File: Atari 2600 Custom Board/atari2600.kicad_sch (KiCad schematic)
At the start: 8 parts, among them SW1 B3F-4050

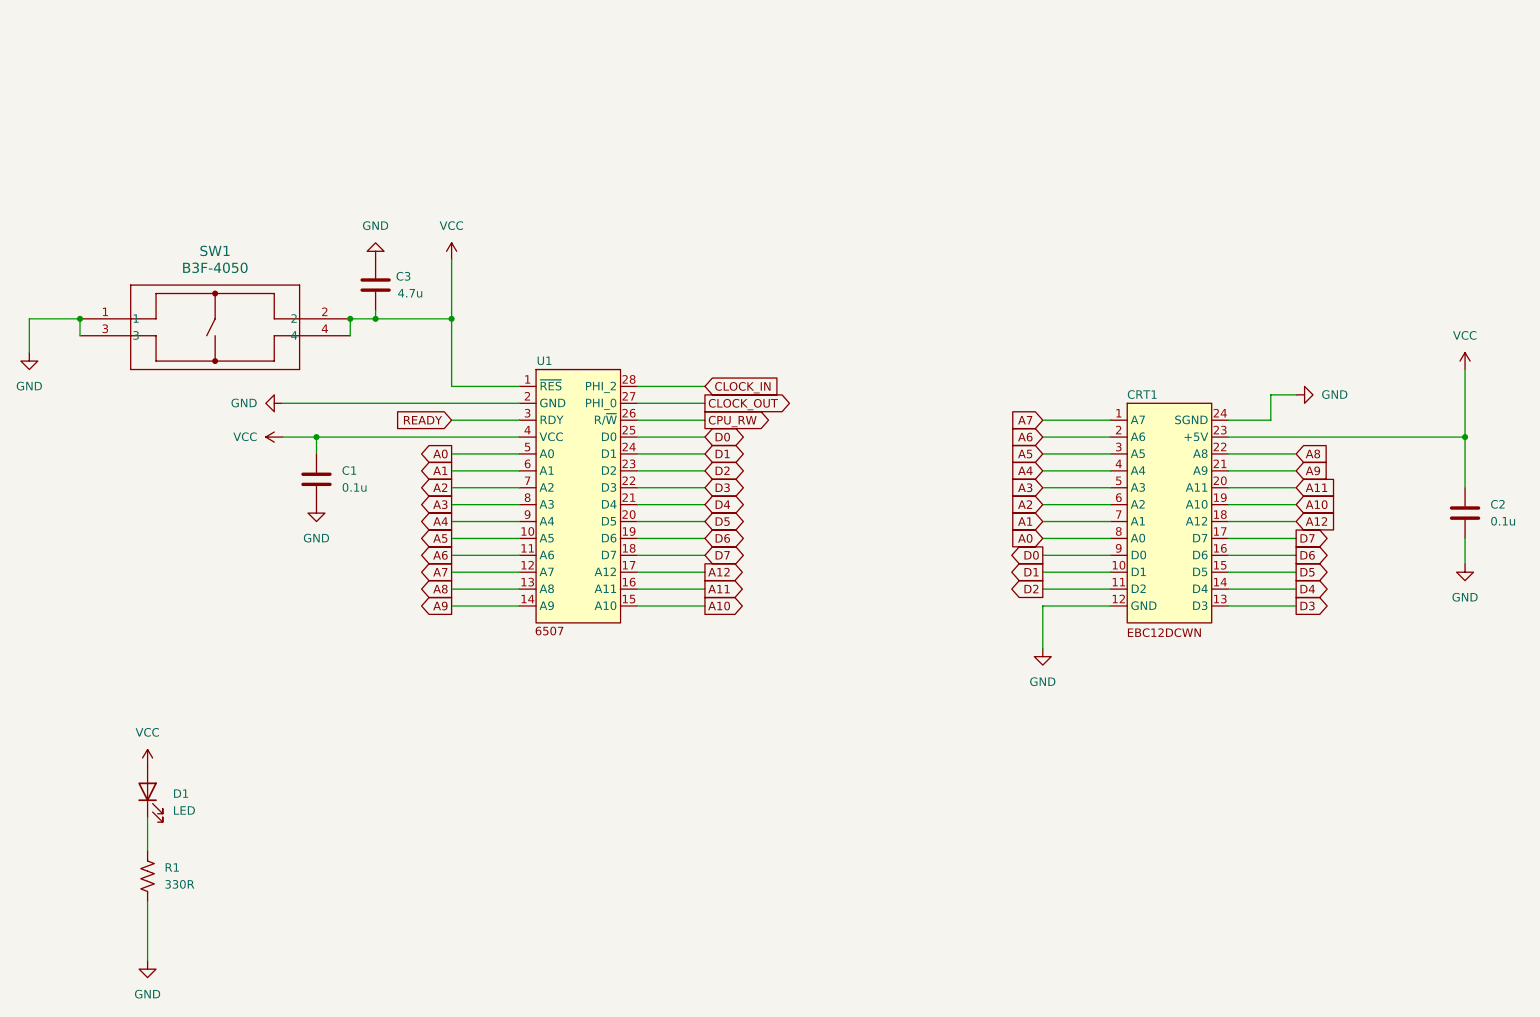
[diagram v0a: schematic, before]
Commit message: Added flat hierarchy schematic pages
Added schematic pages.
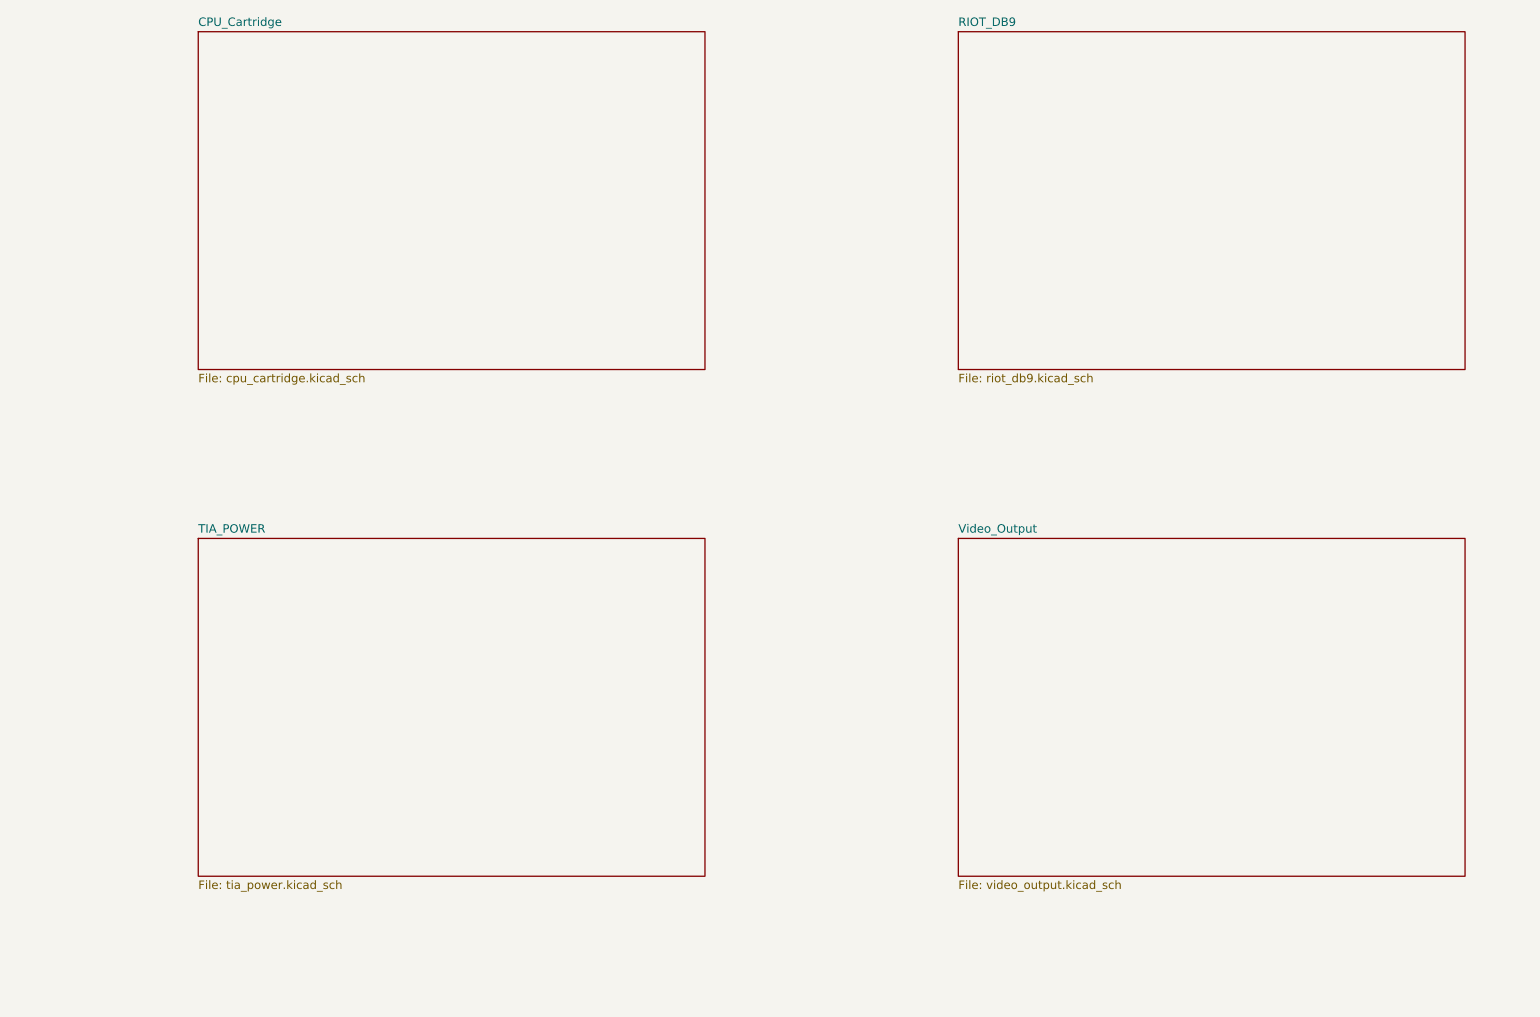
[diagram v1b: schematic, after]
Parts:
- removed C1, C2: 0.1u, symbol Device:C
- removed C3: 4.7u, symbol Device:C
- removed CRT1: ~, symbol 1_atari_library:EBC12DCWN
- removed D1: LED, Diode_SMD:D_MiniMELF_Handsoldering, symbol Device:LED
- removed R1: 330R, Resistor_SMD:R_0805_2012Metric_Pad1.20x1.40mm_HandSolder, symbol Device:R_US
- removed SW1: B3F-4050, SW_B3F-4050_OMR, symbol 1_atari_library:B3F-4050
- removed U1: ~, symbol 1_atari_library:6507
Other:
- added sheet CPU_Cartridge (cpu_cartridge.kicad_sch)
- added sheet RIOT_DB9 (riot_db9.kicad_sch)
- added sheet TIA_POWER (tia_power.kicad_sch)
- added sheet Video_Output (video_output.kicad_sch)
